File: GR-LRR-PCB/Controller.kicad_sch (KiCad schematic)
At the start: 3 parts, among them J1 DF40HC3.5-80DS-0.4V51, J16 Conn_01x30_Pin, J2 DF40HC3.5-80DS-0.4V51

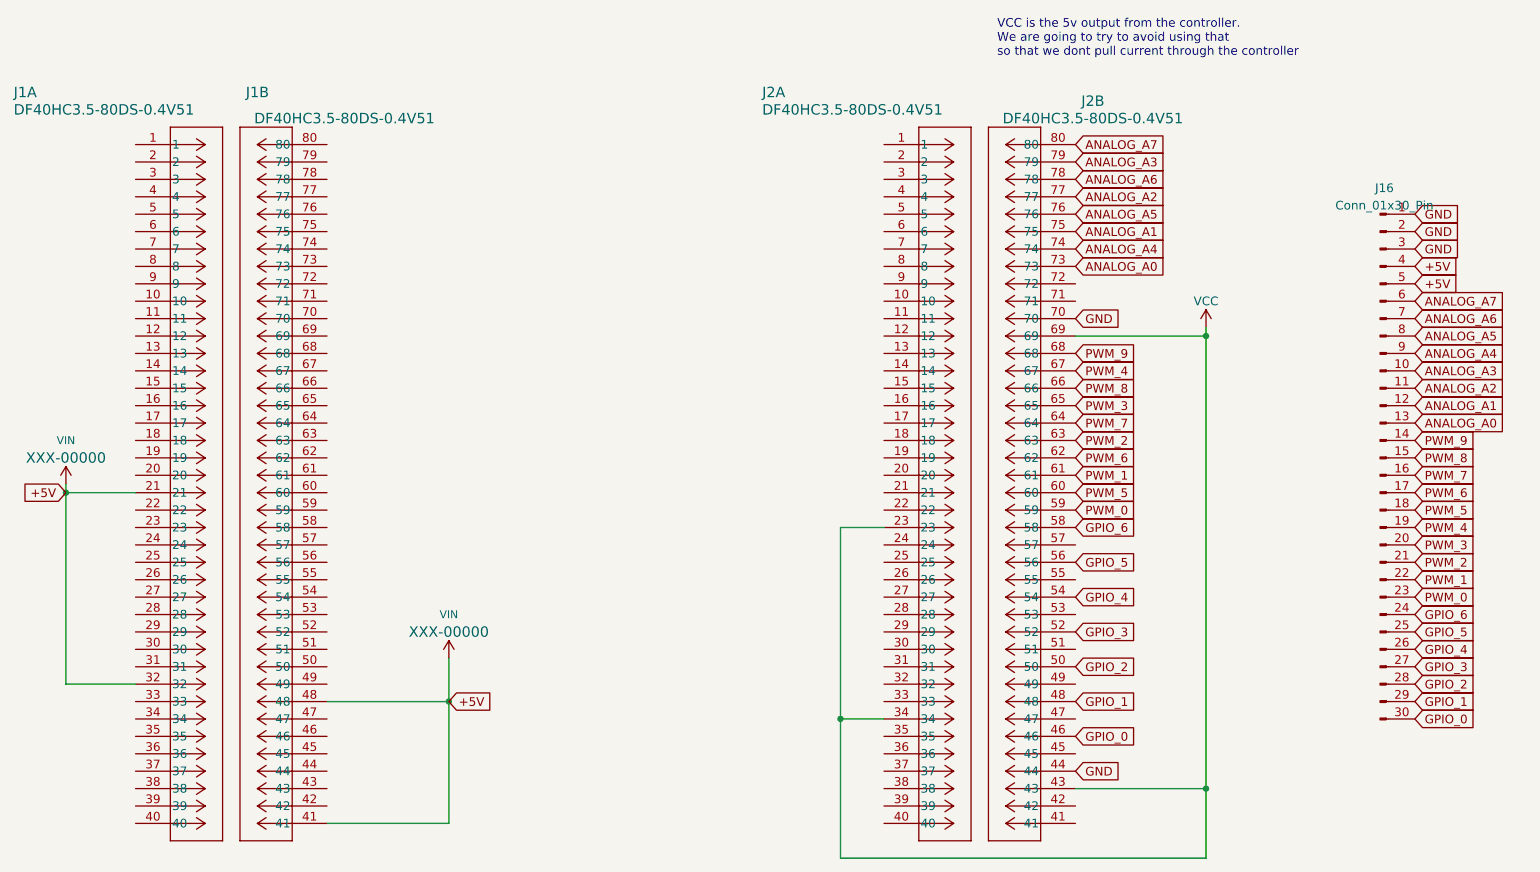
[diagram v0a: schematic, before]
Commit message: new smaller layout
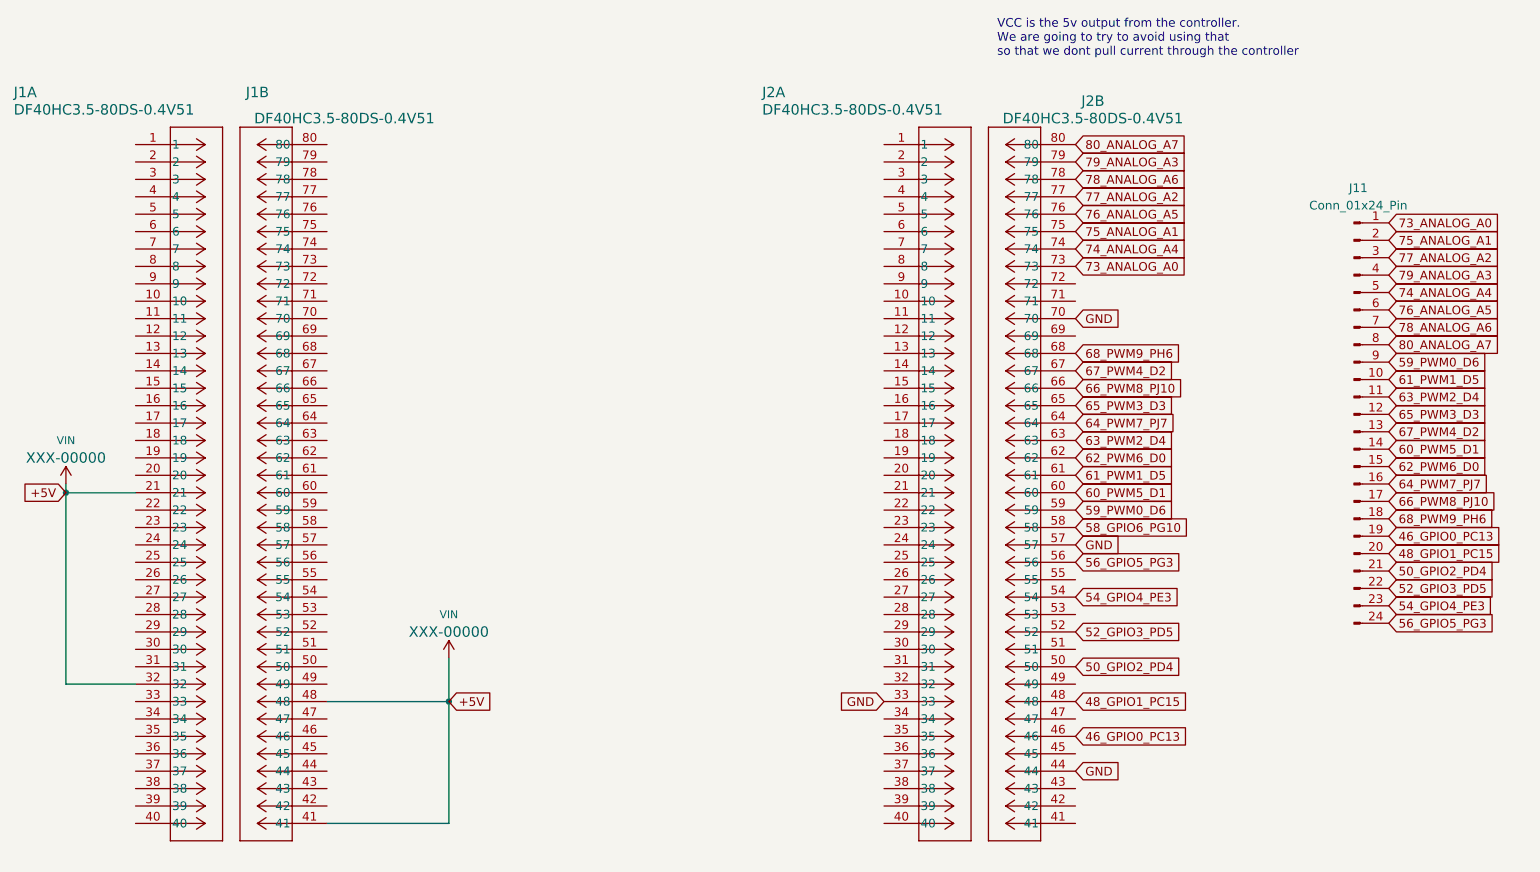
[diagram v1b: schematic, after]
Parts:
- removed J16: Conn_01x30_Pin, Connector_PinHeader_2.54mm:PinHeader_1x30_P2.54mm_Vertical, symbol Connector:Conn_01x30_Pin
- added J11: Conn_01x24_Pin, Connector_PinHeader_2.54mm:PinHeader_1x24_P2.54mm_Vertical, symbol Connector:Conn_01x24_Pin
- J1, J2: footprint DF40HC(3.5)-80DS-0.4V(51):DF40HC3580DS04V58 -> DF40HC3580DS04V58:DF40HC3580DS04V58
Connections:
- net GND: now also J2.33, J2.57
- net ANALOG_A0 renamed 73_ANALOG_A0
- net 73_ANALOG_A0: now also J11.1 (Pin_1)
- net ANALOG_A1 renamed 75_ANALOG_A1
- net 75_ANALOG_A1: now also J11.2 (Pin_2)
- net ANALOG_A2 renamed 77_ANALOG_A2
- net 77_ANALOG_A2: now also J11.3 (Pin_3)
- net ANALOG_A3 renamed 79_ANALOG_A3
- net 79_ANALOG_A3: now also J11.4 (Pin_4)
- net ANALOG_A4 renamed 74_ANALOG_A4
- net 74_ANALOG_A4: now also J11.5 (Pin_5)
- net ANALOG_A5 renamed 76_ANALOG_A5
- net 76_ANALOG_A5: now also J11.6 (Pin_6)
- net ANALOG_A6 renamed 78_ANALOG_A6
- net 78_ANALOG_A6: now also J11.7 (Pin_7)
- net ANALOG_A7 renamed 80_ANALOG_A7
- net 80_ANALOG_A7: now also J11.8 (Pin_8)
- net GPIO_0 renamed 46_GPIO0_PC13
- net 46_GPIO0_PC13: now also J11.19 (Pin_19)
- net GPIO_1 renamed 48_GPIO1_PC15
- net 48_GPIO1_PC15: now also J11.20 (Pin_20)
- net GPIO_2 renamed 50_GPIO2_PD4
- net 50_GPIO2_PD4: now also J11.21 (Pin_21)
- net GPIO_3 renamed 52_GPIO3_PD5
- net 52_GPIO3_PD5: now also J11.22 (Pin_22)
- net GPIO_4 renamed 54_GPIO4_PE3
- net 54_GPIO4_PE3: now also J11.23 (Pin_23)
- net GPIO_5 renamed 56_GPIO5_PG3
- net 56_GPIO5_PG3: now also J11.24 (Pin_24)
- net GPIO_6 renamed 58_GPIO6_PG10
- net PWM_0 renamed 59_PWM0_D6
- net 59_PWM0_D6: now also J11.9 (Pin_9)
- net PWM_1 renamed 61_PWM1_D5
- net 61_PWM1_D5: now also J11.10 (Pin_10)
- net PWM_2 renamed 63_PWM2_D4
- net 63_PWM2_D4: now also J11.11 (Pin_11)
- net PWM_3 renamed 65_PWM3_D3
- net 65_PWM3_D3: now also J11.12 (Pin_12)
- net PWM_4 renamed 67_PWM4_D2
- net 67_PWM4_D2: now also J11.13 (Pin_13)
- net PWM_5 renamed 60_PWM5_D1
- net 60_PWM5_D1: now also J11.14 (Pin_14)
- net PWM_6 renamed 62_PWM6_D0
- net 62_PWM6_D0: now also J11.15 (Pin_15)
- net PWM_7 renamed 64_PWM7_PJ7
- net 64_PWM7_PJ7: now also J11.16 (Pin_16)
- net PWM_8 renamed 66_PWM8_PJ10
- net 66_PWM8_PJ10: now also J11.17 (Pin_17)
- net PWM_9 renamed 68_PWM9_PH6
- net 68_PWM9_PH6: now also J11.18 (Pin_18)
- removed net VCC: J2.23, J2.34, J2.43, J2.69
